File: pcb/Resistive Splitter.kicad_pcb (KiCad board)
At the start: 2 copper layers, 75 x 40 mm, 6 parts, among them J1 SMA 50, J2 SMA 50, J3 SMA 50

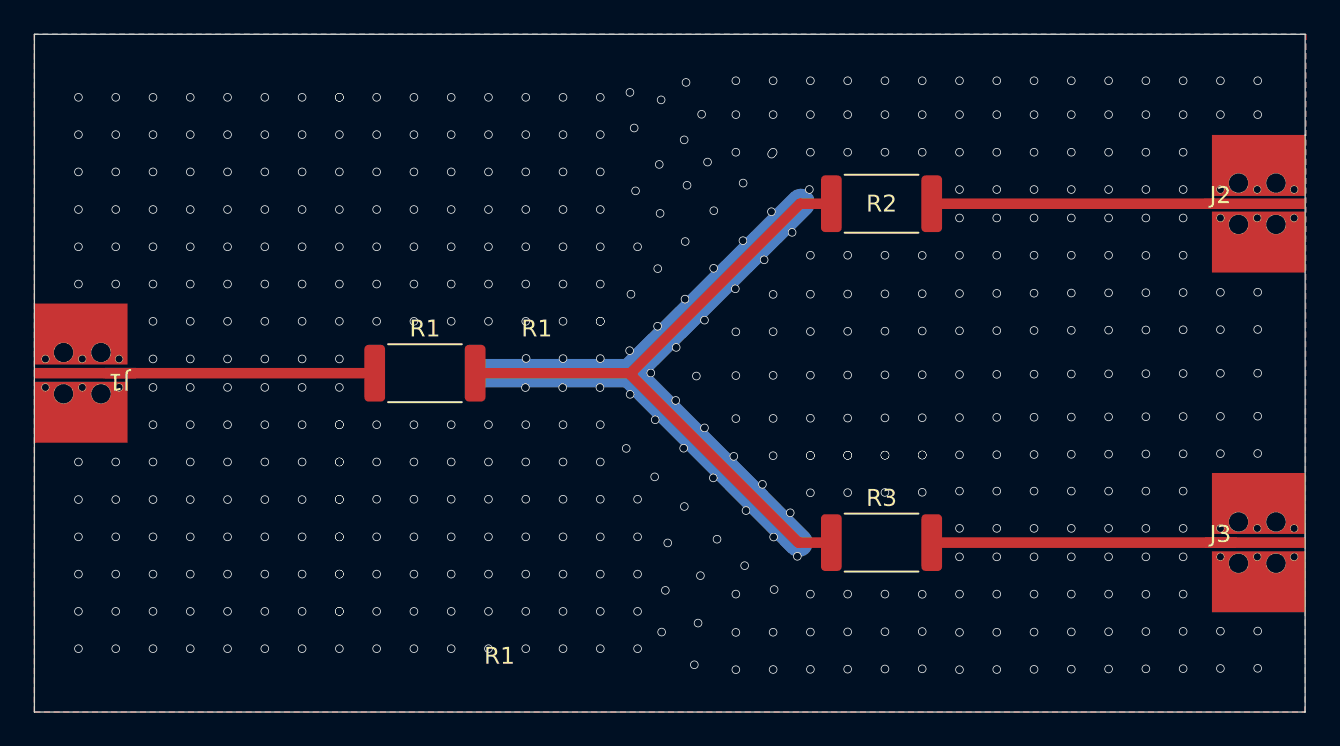
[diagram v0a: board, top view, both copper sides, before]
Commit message: remove repeated top overlay
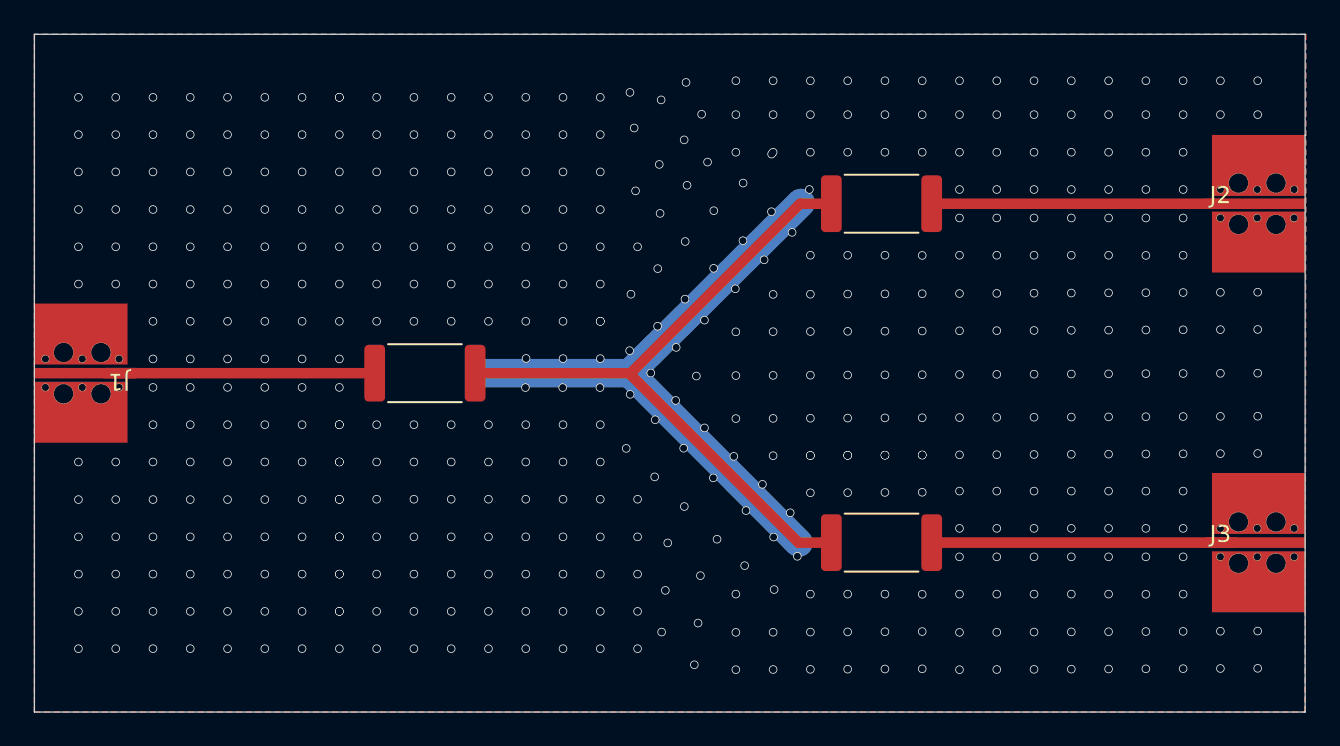
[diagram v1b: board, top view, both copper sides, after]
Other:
- board text removed: "J1"
- board text removed: "R1"
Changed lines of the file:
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@@
 		(tags "resistor")
 		(property "Reference" "R2"
-			(at 0 0 0)
+			(at 0.27 -3.65 0)
 			(layer "F.SilkS")
+			(hide yes)
 			(effects
 				(font
@@
 			(at 0 2.63 0)
 			(layer "F.Fab")
+			(hide yes)
 			(effects
 				(font
@@
 			)
 			(layer "F.Fab")
-		)
-		(fp_text user "${REFERENCE}"
-			(at 0 0 0)
-			(layer "F.Fab")
-			(effects
-				(font
-					(size 1 1)
-					(thickness 0.15)
-				)
-			)
 		)
 		(pad "1" smd roundrect
@@
 			(at 0 -2.63 0)
 			(layer "F.SilkS")
+			(hide yes)
 			(effects
 				(font
@@
 			(at 0 2.63 0)
 			(layer "F.Fab")
+			(hide yes)
 			(effects
 				(font
@@
 			)
 			(layer "F.Fab")
-		)
-		(fp_text user "${REFERENCE}"
-			(at 0 0 0)
-			(layer "F.Fab")
-			(effects
-				(font
-					(size 1 1)
-					(thickness 0.15)
-				)
-			)
 		)
 		(pad "1" smd roundrect
@@
 			(at 0 -2.63 0)
 			(layer "F.SilkS")
+			(hide yes)
 			(effects
 				(font
@@
 			(at 0 2.63 0)
 			(layer "F.Fab")
+			(hide yes)
 			(effects
 				(font
@@
 			)
 			(layer "F.Fab")
-		)
-		(fp_text user "${REFERENCE}"
-			(at -0.05 -5.45 0)
-			(layer "F.Fab")
-			(effects
-				(font
-					(size 1 1)
-					(thickness 0.15)
-				)
-			)
 		)
 		(pad "1" smd roundrect
@@
 		(layer "Edge.Cuts")
 	)
-	(gr_text "R1"
-		(at 27.45 36.69 0)
-		(layer "F.SilkS")
+	(gr_text "75.0 mm"
+		(at 30 51.35 0)
+		(layer "Dwgs.User")
 		(effects
 			(font
@@
 				(thickness 0.15)
 			)
-		)
-	)
-	(gr_text "R1"
-		(at 29.65 17.37 0)
-		(layer "F.SilkS")
+			(justify left bottom)
+		)
+	)
+	(gr_text "40.0 mm"
+		(at 88.95 20.7 0)
+		(layer "Dwgs.User")
 		(effects
 			(font
@@
 				(thickness 0.15)
 			)
-		)
-	)
-	(gr_text "75.0 mm"
-		(at 30 51.35 0)
+			(justify left bottom)
+		)
+	)
+	(gr_text "Layer Stackup\n"
+		(at 160.1 41.35 0)
 		(layer "Dwgs.User")
 		(effects
@@
 		)
 	)
-	(gr_text "40.0 mm"
-		(at 88.95 20.7 0)
+	(gr_text "Top Silkscreen"
+		(at 177 43.5 0)
 		(layer "Dwgs.User")
 		(effects
@@
 		)
 	)
-	(gr_text "Layer Stackup\n"
-		(at 160.1 41.35 0)
+	(gr_text "Top Soldermask (Green)"
+		(at 177 45.5 0)
 		(layer "Dwgs.User")
 		(effects
@@
 		)
 	)
-	(gr_text "Top Silkscreen"
-		(at 177 43.5 0)
+	(gr_text "Top Layer 1 oz (35um) Copper\n"
+		(at 177 47.5 0)
 		(layer "Dwgs.User")
 		(effects
@@
 		)
 	)
-	(gr_text "Top Soldermask (Green)"
-		(at 177 45.5 0)
+	(gr_text "RO4350B 0.51mm (Dk=3.48, Df=0.0037)"
+		(at 177 49.5 0)
 		(layer "Dwgs.User")
 		(effects
@@
 		)
 	)
-	(gr_text "Top Layer 1 oz (35um) Copper\n"
-		(at 177 47.5 0)
+	(gr_text "Bottom Layer 1 oz (35um) Copper\n"
+		(at 177 51.5 0)
 		(layer "Dwgs.User")
 		(effects
@@
 		)
 	)
-	(gr_text "RO4350B 0.51mm (Dk=3.48, Df=0.0037)"
-		(at 177 49.5 0)
+	(gr_text "Bottom Soldermask (Green)"
+		(at 177 53.5 0)
 		(layer "Dwgs.User")
 		(effects
@@
 		)
 	)
-	(gr_text "Bottom Layer 1 oz (35um) Copper\n"
-		(at 177 51.5 0)
+	(gr_text "Pad Finish ENIG (1 U{dblquote})\n\n"
+		(at 180.5 66.65 0)
 		(layer "Dwgs.User")
 		(effects
@@
 		)
 	)
-	(gr_text "Bottom Soldermask (Green)"
-		(at 177 53.5 0)
-		(layer "Dwgs.User")
-		(effects
-			(font
-				(size 1 1)
-				(thickness 0.15)
-			)
-			(justify left bottom)
-		)
-	)
-	(gr_text "Pad Finish ENIG (1 U{dblquote})\n\n"
-		(at 180.5 66.65 0)
-		(layer "Dwgs.User")
-		(effects
-			(font
-				(size 1 1)
-				(thickness 0.15)
-			)
-			(justify left bottom)
-		)
-	)
-	(gr_text "J1"
-		(at 2.75 8.98 0)
-		(layer "F.Fab")
-		(effects
-			(font
-				(size 1 1)
-				(thickness 0.15)
-			)
-		)
-	)
-	(gr_text "J1"
-		(at 2.75 26.1 0)
-		(layer "F.Fab")
-		(effects
-			(font
-				(size 1 1)
-				(thickness 0.15)
-			)
-		)
-	)
-	(gr_text "J1"
-		(at 2.75 34.92 0)
-		(layer "F.Fab")
-		(effects
-			(font
-				(size 1 1)
-				(thickness 0.15)
-			)
-		)
-	)
-	(gr_text "J1"
-		(at 7.15 8.98 0)
-		(layer "F.Fab")
-		(effects
-			(font
-				(size 1 1)
-				(thickness 0.15)
-			)
-		)
-	)
-	(gr_text "J1"
-		(at 7.15 26.1 0)
-		(layer "F.Fab")
-		(effects
-			(font
-				(size 1 1)
-				(thickness 0.15)
-			)
-		)
-	)
-	(gr_text "J1"
-		(at 7.15 34.92 0)
-		(layer "F.Fab")
-		(effects
-			(font
-				(size 1 1)
-				(thickness 0.15)
-			)
-		)
-	)
-	(gr_text "J1"
-		(at 7.15 37.12 0)
-		(layer "F.Fab")
-		(effects
-			(font
-				(size 1 1)
-				(thickness 0.15)
-			)
-		)
-	)
-	(gr_text "J1"
-		(at 18.15 8.98 0)
-		(layer "F.Fab")
-		(effects
-			(font
-				(size 1 1)
-				(thickness 0.15)
-			)
-		)
-	)
-	(gr_text "J1"
-		(at 18.15 17.8 0)
-		(layer "F.Fab")
-		(effects
-			(font
-				(size 1 1)
-				(thickness 0.15)
-			)
-		)
-	)
-	(gr_text "J1"
-		(at 18.15 28.3 0)
-		(layer "F.Fab")
-		(effects
-			(font
-				(size 1 1)
-				(thickness 0.15)
-			)
-		)
-	)
-	(gr_text "J1"
-		(at 18.15 37.12 0)
-		(layer "F.Fab")
-		(effects
-			(font
-				(size 1 1)
-				(thickness 0.15)
-			)
-		)
-	)
-	(gr_text "R1"
-		(at 27.4 33.87 0)
-		(layer "F.Fab")
-		(effects
-			(font
-				(size 1 1)
-				(thickness 0.15)
-			)
-		)
-	)
-	(gr_text "R1"
-		(at 29.6 14.55 0)
-		(layer "F.Fab")
-		(effects
-			(font
-				(size 1 1)
-				(thickness 0.15)
-			)
-		)
-	)
